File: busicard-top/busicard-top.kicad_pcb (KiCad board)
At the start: 2 copper layers, 70 x 46 mm, 10 parts

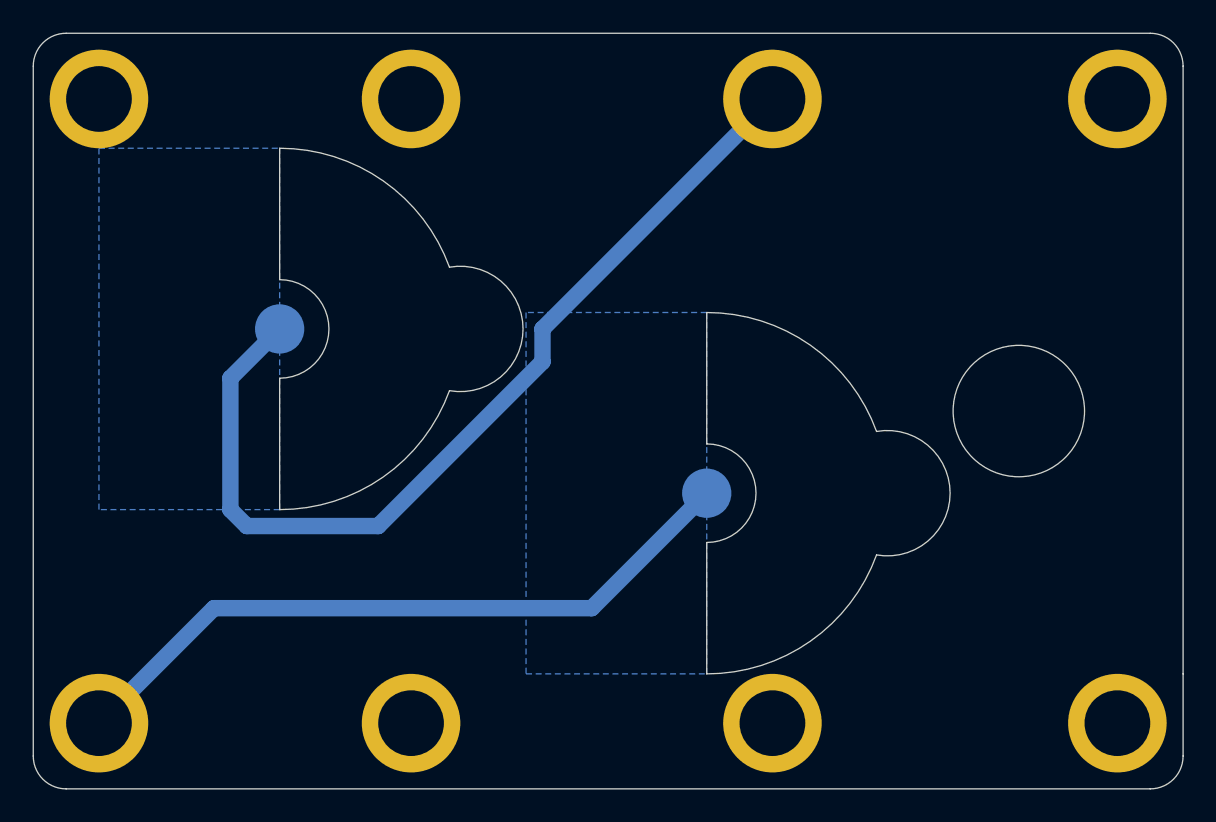
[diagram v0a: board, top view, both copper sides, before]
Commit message: More steps to production
- add slik
- add paste to battery pads
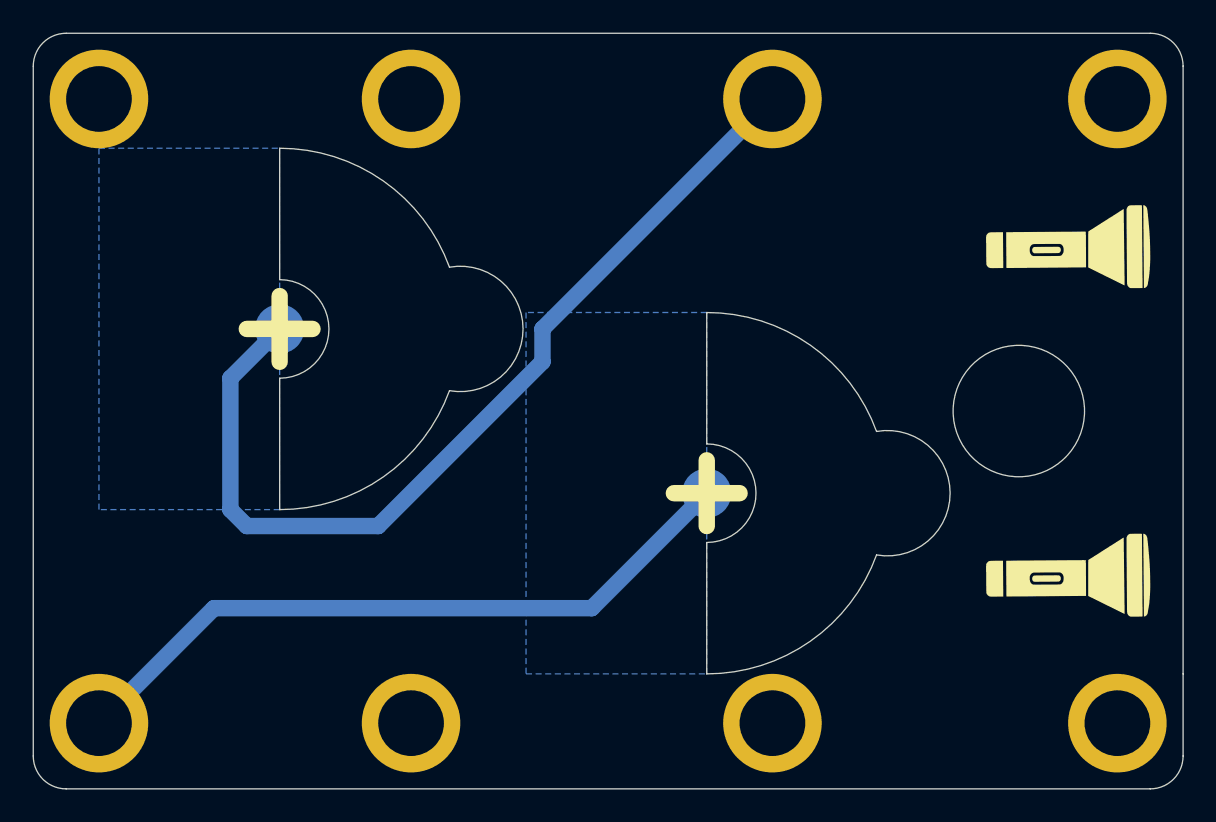
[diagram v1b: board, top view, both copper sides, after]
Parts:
- added G***: LOGO, lib:flashlight-small, F.Cu at (193.0, 110.0)
- added G***: LOGO, lib:flashlight-small, F.Cu at (193.0, 90.0)
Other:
- board text added: "busicard-top @TomKeddie May2024"
- board text added: "image from vecteezy.com thickness should be 0.8mm"

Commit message: Add assembly holes and batch number on silkscreen
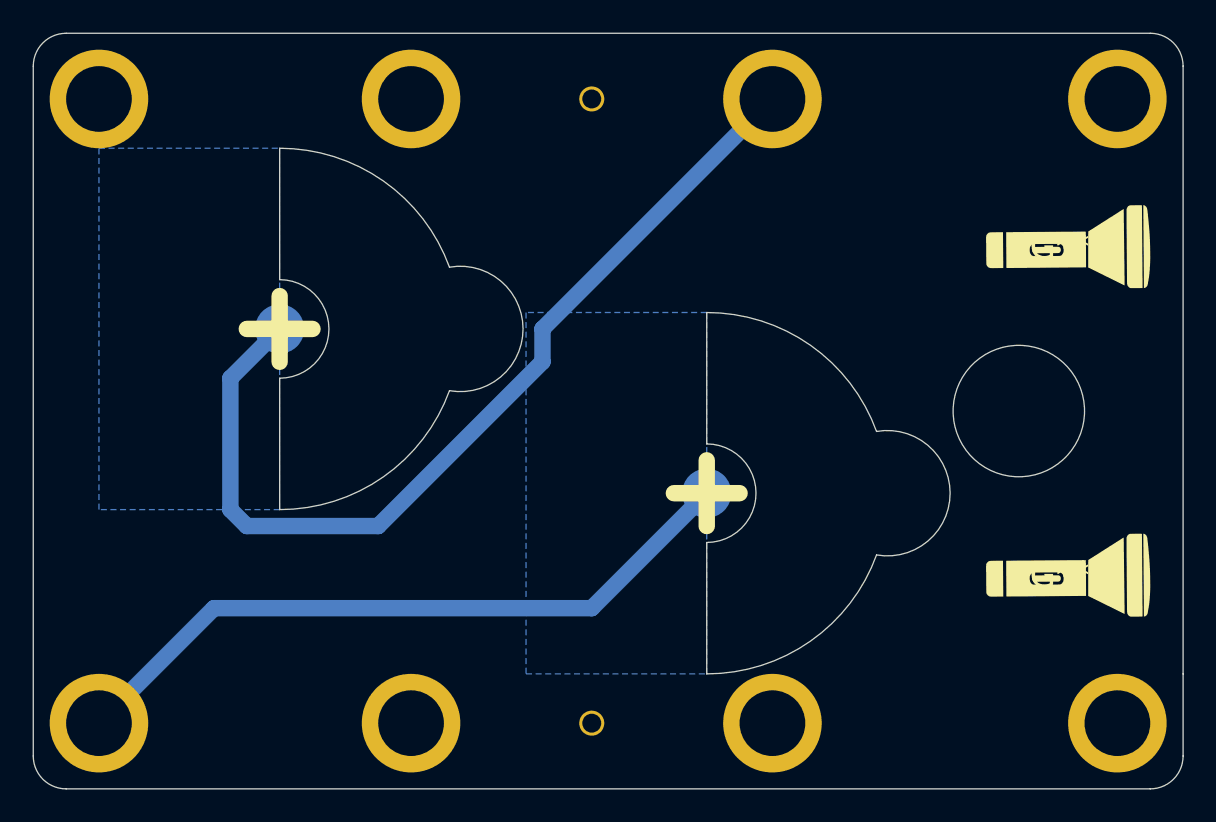
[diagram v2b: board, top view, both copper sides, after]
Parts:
- added H1: mech-only-no-pins, lib:JLC_ASSEMBLY_HOLE, F.Cu at (164.0, 81.0)
- added H2: mech-only-no-pins, lib:JLC_ASSEMBLY_HOLE, F.Cu at (164.0, 119.0)
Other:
- board text added: "JLCJLCJLCJLC"

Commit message: busicard-top: enlarge battery opening
move all mount points 0.5mm towards edges
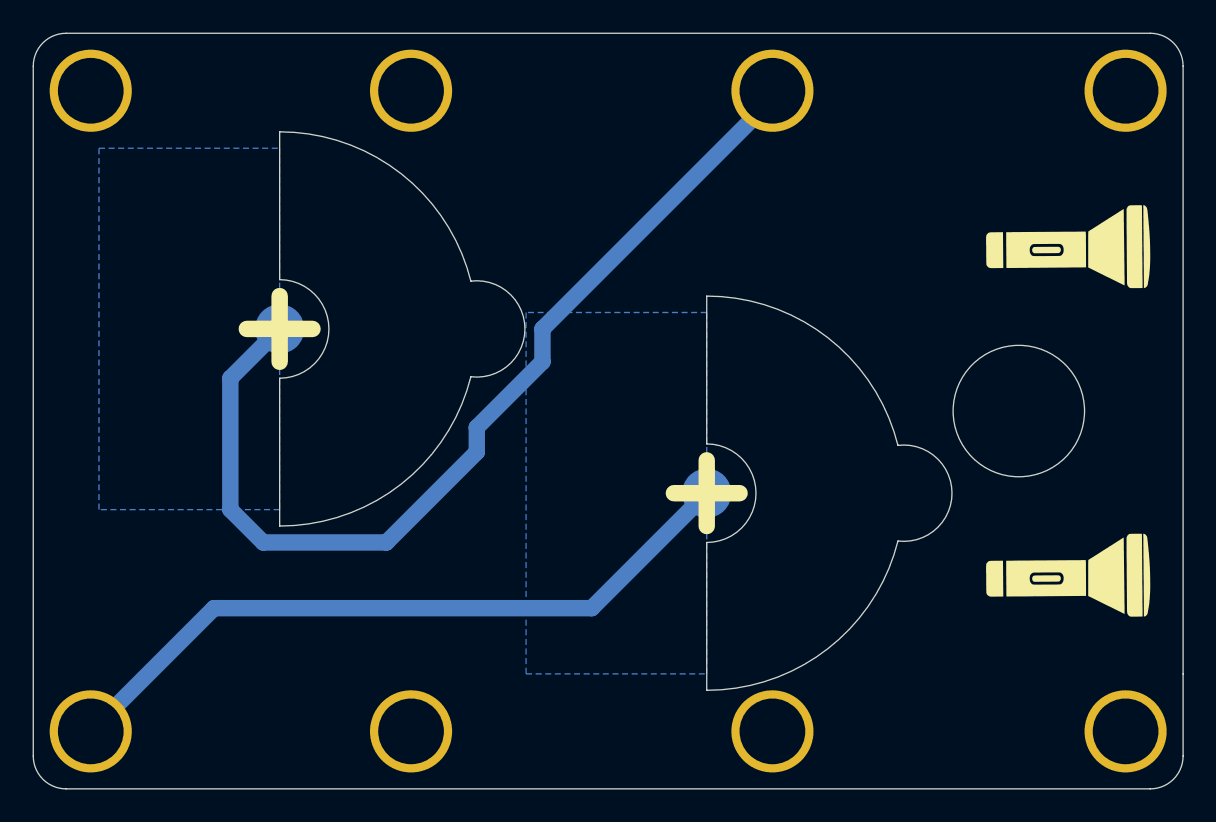
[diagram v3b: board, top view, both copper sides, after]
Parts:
- removed H1, H2: mech-only-no-pins, lib:JLC_ASSEMBLY_HOLE
- moved TP10 0.71 mm to (133.5, 80.5)
- moved TP4 0.71 mm to (133.5, 119.5)
- moved TP5 0.71 mm to (196.5, 119.5)
- moved TP6 0.71 mm to (196.5, 80.5)
- moved TP1 0.50 mm to (175.0, 80.5)
- moved TP7 0.50 mm to (153.0, 119.5)
- moved TP8 0.50 mm to (153.0, 80.5)
- moved TP9 0.50 mm to (175.0, 119.5)
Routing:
- net /BATT1+: track 57.6 -> 59.3 mm
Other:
- outline, holes or cut-outs redrawn
